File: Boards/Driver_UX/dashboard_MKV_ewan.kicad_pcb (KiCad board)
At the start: 4 copper layers, 58.5 x 37.5 mm, 68 parts, among them J1 MM_F_VT_10, J2 MM_F_VT_20, J4 CONN_02X03, J5 CONN_02X03, Q1 SSM3K333R, U1 ATMEGA16M1, U101 TPS560430YF, U3 ATmega328P-AU, U4 CAN_Transceiver, Y1 Crystal_SMD, Y2 Crystal_SMD

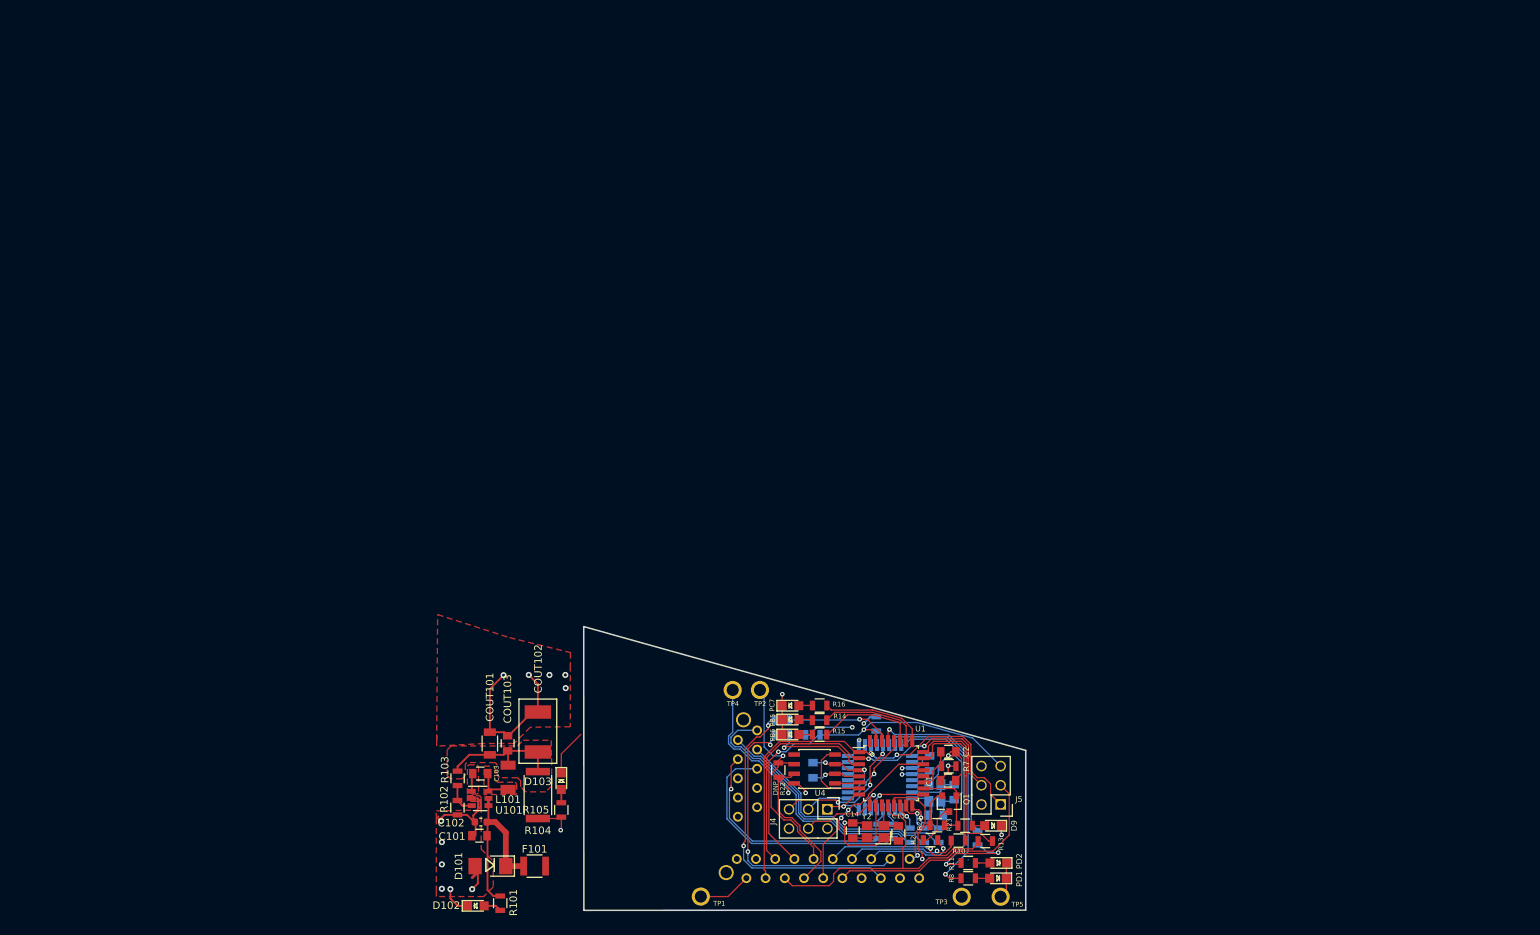
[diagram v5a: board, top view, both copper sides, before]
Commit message: Added 3A Buck Variant
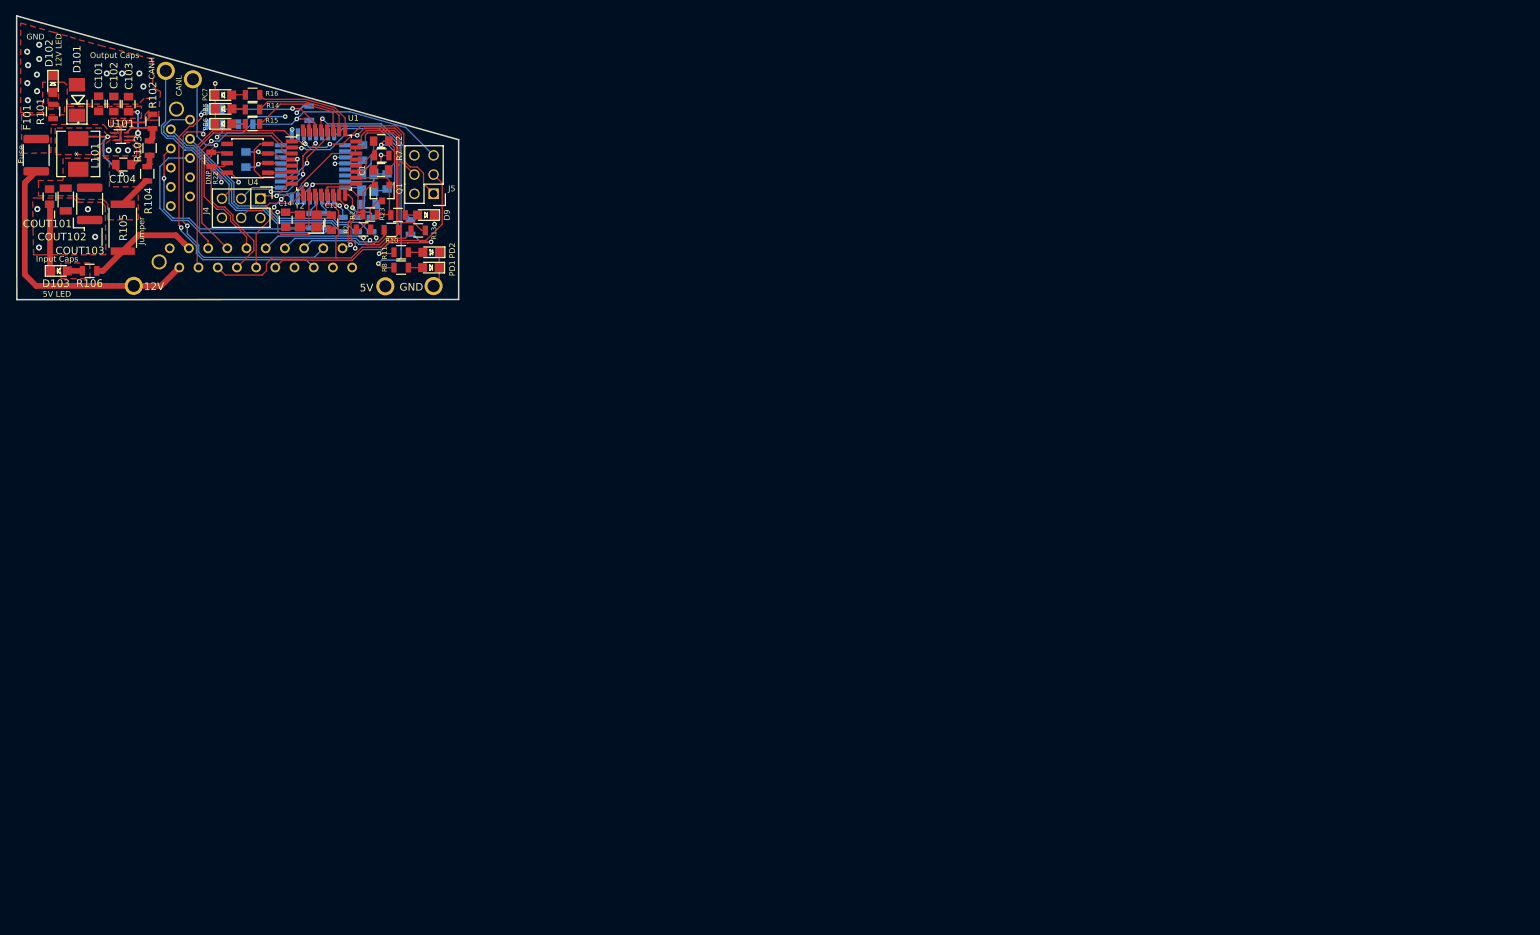
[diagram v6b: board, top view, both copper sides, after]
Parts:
- added C104: C_0.1uF, footprints:C_0805_OEM, F.Cu at (41.2, 48.1)
- added R106: R_200, footprints:R_0805_OEM, F.Cu at (36.7, 62.2)
- C102: value C_2.2uF -> C_10uF_25V; footprint footprints:C_0603_1608Metric -> footprints:C_0805_OEM
- C103: value C_0.1uF -> C_10uF_25V
- COUT101: value C_22uF -> C_10uF; footprint footprints:C_1206_OEM -> footprints:C_0805_OEM
- COUT102: value C_33uF -> C_22uF; footprint footprints:Fuse_1812 -> footprints:C_1206_OEM
- COUT103: value C_47uF -> C_33uF; footprint footprints:C_0805_OEM -> footprints:C_1812_4532Metric
- F101: value F_500mA_16V -> F_2.6A_16V; footprint footprints:Fuse_1210 -> footprints:Fuse_1812_4532Metric
- L101: value L_100uH -> L_4.7uH; footprint footprints:L_100uH -> footprints:IHLP2020BZER4R7M11-L_4.7_3.2A
- R101: value R_200 -> R_1K
- R102: value R_25K -> R_10K
- R103: value R_100K -> R_51.1K
- R104: value R_0_2512 -> R_22K; footprint footprints:R_2512_OEM -> footprints:R_0805_OEM
- R105: value R_200 -> R_0_2512; footprint footprints:R_0805_OEM -> footprints:R_2512_OEM
- U101: value TPS560430YF -> TPS563231; footprint footprints:SOT-23-6_OEM -> Package_TO_SOT_SMD:SOT-563
- moved D102 122.3 mm to (31.9, 37.5), turned to 270 degrees
- moved R101 120.3 mm to (31.9, 41.1), turned to 90 degrees
- moved D101 115.2 mm to (35.0, 39.6), turned to 90 degrees
- moved F101 114.9 mm to (29.7, 46.9), turned to 90 degrees
- moved TP3 111.1 mm to (75.8, 64.2)
- moved TP4 111.1 mm to (46.8, 35.7)
- moved C10 110.2 mm to (73.6, 53.4)
- moved C13 110.2 mm to (68.7, 55.8)
- moved C15 110.2 mm to (57.4, 47.5)
- moved C2 110.2 mm to (75.3, 45.0)
- moved C9 110.2 mm to (76.1, 50.4)
- moved D3 110.2 mm to (81.9, 61.8)
- moved D4 110.2 mm to (81.9, 59.7)
- moved J2 110.2 mm to (52.4, 59.2)
- moved R10 110.2 mm to (76.6, 56.8)
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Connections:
- C103 pad 1: Net-(C103-Pad1) -> Net-(C101-Pad1)
- C103 pad 2: Net-(C103-Pad2) -> GND
- COUT102 pad 1: Net-(COUT101-Pad1) -> GND
- COUT102 pad 2: GND -> Net-(COUT101-Pad1)
- F101 pad 1: Net-(C101-Pad1) -> /12V
- F101 pad 2: /12V -> Net-(C101-Pad1)
- L101 pad 1: Net-(C103-Pad2) -> Net-(C104-Pad1)
- R103 pad 1: Net-(COUT101-Pad1) -> Net-(R103-Pad1)
- R104 pad 2: VCC -> Net-(R103-Pad1)
- R105 pad 2: Net-(D103-Pad2) -> Net-(COUT101-Pad1)
- U101 pad 1: Net-(C103-Pad1) -> Net-(C101-Pad1)
- U101 pad 2: GND -> Net-(C104-Pad1)
- U101 pad 3: Net-(R102-Pad1) -> GND
- U101 pad 4: Net-(C101-Pad1) -> Net-(C104-Pad2)
- U101 pad 6: Net-(C103-Pad2) -> Net-(R102-Pad1)
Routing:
- net GND: track 118.8 -> 87.8 mm, vias 19 -> 27
- net /12V: track 7.04 -> 36.3 mm
- net Net-(C101-Pad1): track 24.1 -> 5.73 mm, vias 0 -> 2
- net Net-(COUT101-Pad1): track 17.3 -> 4.38 mm
- net Net-(C104-Pad1): track 0.00 -> 12.8 mm, vias 0 -> 2
- net VCC: track 44.9 -> 53.7 mm, vias 7 -> 6
- net Net-(C103-Pad2): track 5.44 -> 0.00 mm
- net Net-(C104-Pad2): track 0.00 -> 5.30 mm
- net Net-(D102-Pad2): track 2.67 -> 0.00 mm
- net Net-(C103-Pad1): track 2.39 -> 0.00 mm
- net Net-(R103-Pad1): track 0.00 -> 1.63 mm
- net Net-(R102-Pad1): track 4.18 -> 5.71 mm
- net /RJLED1: track 39.9 -> 38.4 mm
- net Net-(R8-Pad2): track 31.2 -> 32.5 mm
- net /RJLED2: track 39.3 -> 38.1 mm
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- added copper zone on F.Cu, net Net-(C101-Pad1)
- added copper zone on F.Cu, net Net-(C104-Pad1)
- added copper zone on F.Cu, net Net-(D102-Pad2)
- added copper zone on F.Cu, net Net-(D103-Pad2)
- removed copper zone on F.Cu, net Net-(C103-Pad1)
- removed copper zone on F.Cu, net Net-(C103-Pad2)
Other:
- board text added: "12V LED"
- board text added: "5V LED"
- board text added: "Fuse"
- board text added: "GND"
- board text added: "Input Caps"
- board text added: "Jumper"
- board text added: "Output Caps"
